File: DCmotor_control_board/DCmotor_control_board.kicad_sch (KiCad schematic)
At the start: 22 parts, among them J1 Conn_01x02_Pin, J10 Conn_01x04_Pin, J2 Conn_01x02_Pin, J7 Conn_01x02_Pin, U1 TB67H450FNG_EL, U3 L7805CV

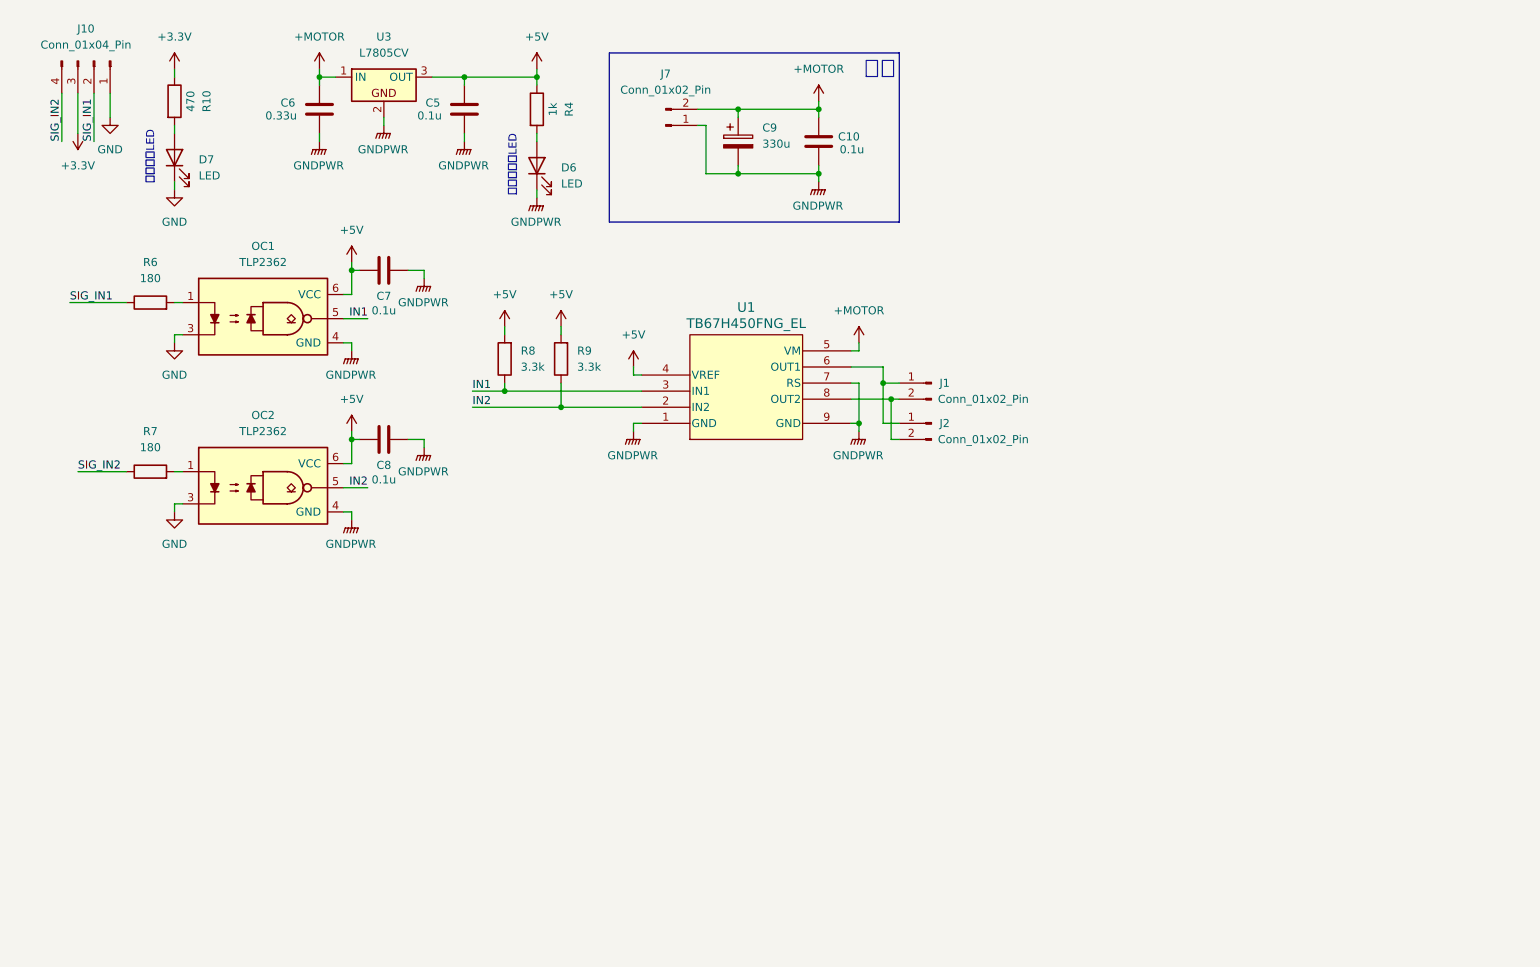
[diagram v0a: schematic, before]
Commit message: モータドライバ回路　回路図改良，フォトカプラの変更等
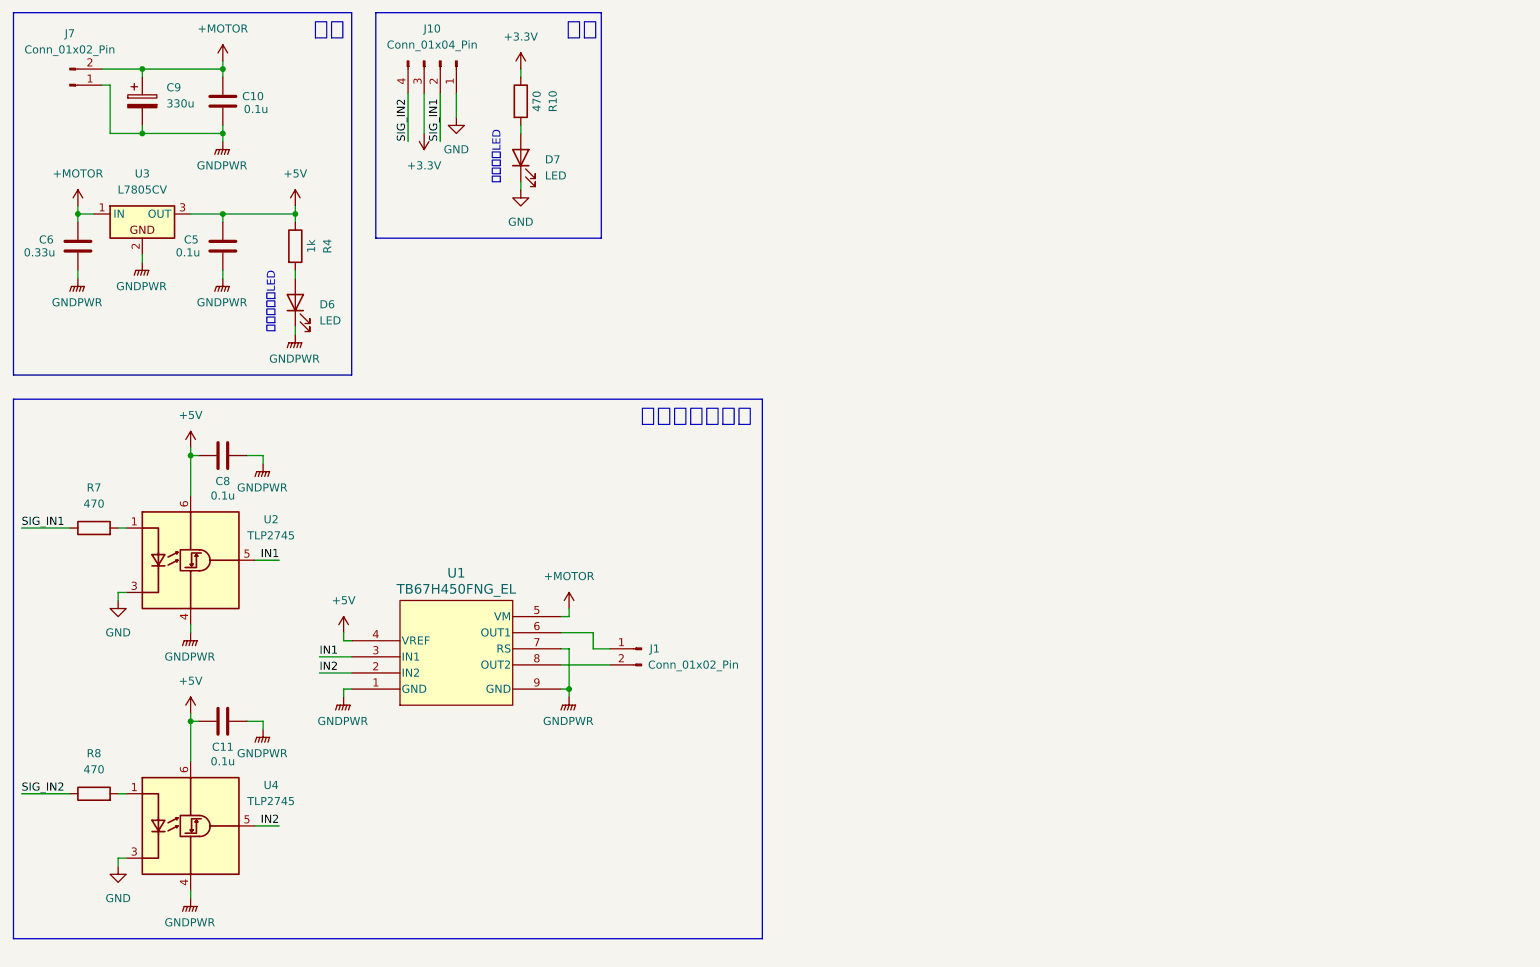
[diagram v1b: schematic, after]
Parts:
- removed C7: 0.1u, Capacitor_THT:C_Disc_D5.0mm_W2.5mm_P2.50mm, symbol Device:C
- removed J2: Conn_01x02_Pin, OU_connector:DF1E-2P-2.5DS, symbol Connector:Conn_01x02_Pin
- removed OC1, OC2: TLP2362, PCM_Package_SO_AKL:SO-5_4.4x3.6mm_P1.27mm, symbol PCM_Optocoupler_Logic_AKL:TLP2362
- removed R6: 180, Resistor_THT:R_Axial_DIN0207_L6.3mm_D2.5mm_P2.54mm_Vertical, symbol Device:R
- removed R9: 3.3k, Resistor_THT:R_Axial_DIN0207_L6.3mm_D2.5mm_P2.54mm_Vertical, symbol Device:R
- added C11: 0.1u, Capacitor_THT:C_Disc_D5.0mm_W2.5mm_P2.50mm, symbol Device:C
- added U2, U4: TLP2745, Package_SO:SO-6L_10x3.84mm_P1.27mm, symbol Isolator:TLP2745
- R7: value 180 -> 470; Buy_URL https://akizukidenshi.com/catalog/g/g125181/ -> https://akizukidenshi.com/catalog/g/g125471/
- R8: value 3.3k -> 470; Buy_URL https://akizukidenshi.com/catalog/g/g125332/ -> https://akizukidenshi.com/catalog/g/g125471/
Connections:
- net +5V: now also C11.2, U2.6 (VDD), U4.6 (VDD); no longer R8.2
- net GND: now also U2.3 (K), U4.3 (K)
- net GNDPWR: now also C11.1, U2.4 (GND), U4.4 (GND)
- net IN1: now also U2.5 (VO); no longer R8.1
- net IN2: now also U4.5 (VO)
- net SIG_IN1: now also R7.1
- net SIG_IN2: now also R8.1; no longer R7.1
- net at R7.2: now also U2.1 (A)
- new net: R8.2, U4.1 (A)
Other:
- note added: "モータドライバ"
- note added: "信号"
- moved on the sheet: C10, C5, C6, C8, C9, D6, D7, J1, J10, J7, R10, R4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

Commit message: モータドライバ基板　モータドライバを1系統から2系統に変更
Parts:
- removed D7: LED, LED_THT:LED_D5.0mm, symbol Device:LED
- removed R10: 470, Resistor_THT:R_Axial_DIN0207_L6.3mm_D2.5mm_P2.54mm_Vertical, symbol Device:R
- added C7, C8: 0.1u, Capacitor_THT:C_Disc_D5.0mm_W2.5mm_P2.50mm, symbol Device:C
- added J4: Conn_01x04_Pin, OU_connector:DF1E-4P-2.5DS, symbol Connector:Conn_01x04_Pin
- added J5: Conn_01x02_Pin, OU_connector:DF1E-2P-2.5DS, symbol Connector:Conn_01x02_Pin
- added R4, R5: 470, Resistor_THT:R_Axial_DIN0207_L6.3mm_D2.5mm_P2.54mm_Vertical, symbol Device:R
- added U5, U6: TLP2745, Package_SO:SO-6L_10x3.84mm_P1.27mm, symbol Isolator:TLP2745
- added U7: TB67H450FNG_EL, OU_Power:P-HSOP8-0405-1p27-002_TOS-L, symbol OU_Power:TB67H450FNG_EL
- renumbered C6 to C1, C9 to C2, C10 to C3, C5 to C4, C8 to C5, C11 to C6, D6 to D1, J7 to J1, J10 to J2, J1 to J3, R7 to R1, R8 to R2, R4 to R3, U3 to U1, U4 to U3, U1 to U4
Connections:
- net +5V: now also C7.2, C8.2, U5.6 (VDD), U6.6 (VDD), U7.4 (VREF)
- net +MOTOR: now also U7.5 (VM)
- net GNDPWR: now also C7.1, C8.1, U5.4 (GND), U6.4 (GND), U7.1 (GND), U7.7 (RS), U7.9 (GND)
- net +3.3V: no longer names the net of J2.3 (Pin_3)
- net GND renamed GND1
- net IN1 renamed IN1_1
- net IN2 renamed IN1_2
- new net: J5.1 (Pin_1), U7.6 (OUT1)
- new net: J5.2 (Pin_2), U7.8 (OUT2)
- new net: R5.2, U6.1 (A)
- new net: R4.2, U5.1 (A)
- new net GND2: J4.1 (Pin_1), U5.3 (K), U6.3 (K)
- new net IN2_1: U5.5 (VO), U7.3 (IN1)
- new net IN2_2: U6.5 (VO), U7.2 (IN2)
- new net SIG_IN3: J4.2 (Pin_2), R4.1
- new net SIG_IN4: J4.4 (Pin_4), R5.1
- no-connect marks 0 -> 2
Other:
- note added: "モータドライバ CH1"
- note added: "モータドライバ CH2"
- note removed: "モータドライバ"
- note removed: "制御電源LED"
- moved on the sheet: C5, C6, J3, R1, R2, U2, U3, U4

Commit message: モータドライバ基板　基板完成，ver 0.1
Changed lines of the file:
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@@
-		)
-	)
-	(label "IN1_2"
-		(at 64.77 73.66 0)
-		(effects
-			(font
-				(size 1.27 1.27)
-			)
-			(justify left bottom)
 		)
 	)

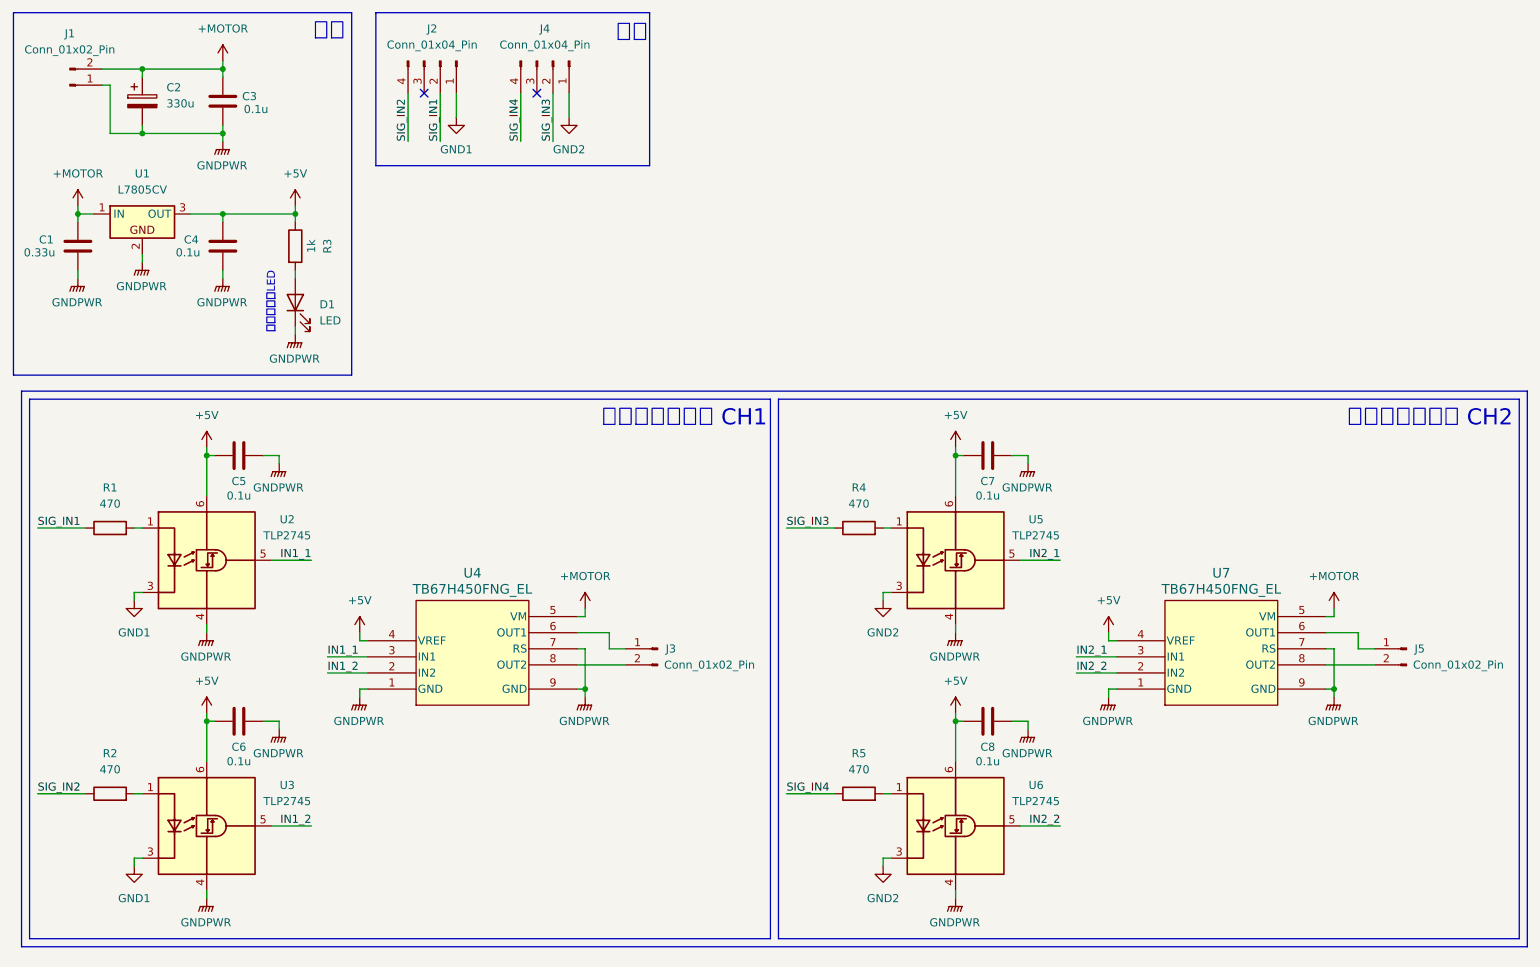
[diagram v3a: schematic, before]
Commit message: モータドライバ基板　TLP2745のURLを追加
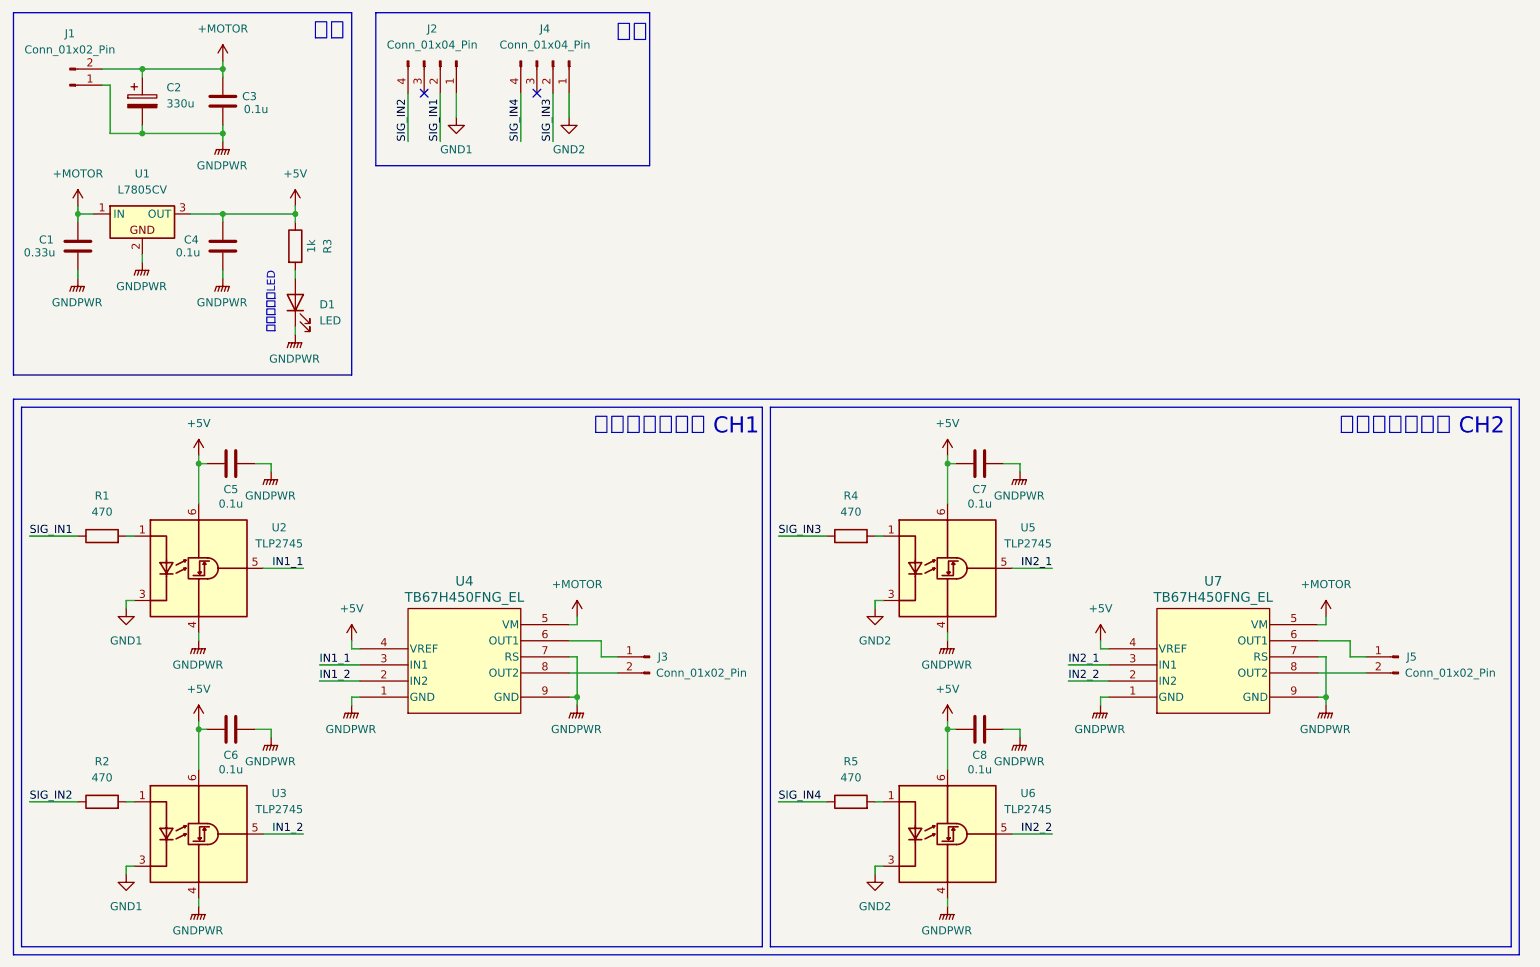
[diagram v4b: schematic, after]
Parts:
- U2, U3, U5, U6: Buy_URL (none) -> https://akizukidenshi.com/catalog/g/g118360/
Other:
- moved on the sheet: C5, C6, C7, C8, J3, J5, R1, R2, R4, R5, U2, U3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

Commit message: モータドライバ基板　シルクを一部修正，ver 1.0
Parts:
- renumbered J4 to J3, J3 to J4
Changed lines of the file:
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@@
 		(dnp no)
 		(fields_autoplaced yes)
-		(property "Reference" "#PWR022"
+		(property "Reference" "#PWR025"
 			(at 161.29 87.63 0)
 			(hide yes)
@@
 			(project "DCmotor_control_board"
 				(path "/99a91a5e-5cbb-4f6e-aa08-d3fc2ac4ed72"
-					(reference "#PWR022")
+					(reference "#PWR025")
 					(unit 1)
 				)
@@
 		(dnp no)
 		(fields_autoplaced yes)
-		(property "Reference" "#PWR020"
+		(property "Reference" "#PWR019"
 			(at 83.82 36.83 0)
 			(hide yes)
@@
 			(project "DCmotor_control_board"
 				(path "/99a91a5e-5cbb-4f6e-aa08-d3fc2ac4ed72"
-					(reference "#PWR020")
+					(reference "#PWR019")
 					(unit 1)
 				)
@@
 		(in_pos_files yes)
 		(dnp no)
-		(property "Reference" "J3"
+		(property "Reference" "J4"
 			(at 115.57 115.57 0)
 			(show_name no)
@@
 			(project "DCmotor_control_board"
 				(path "/99a91a5e-5cbb-4f6e-aa08-d3fc2ac4ed72"
-					(reference "J3")
+					(reference "J4")
 					(unit 1)
 				)
@@
 		(dnp no)
 		(fields_autoplaced yes)
-		(property "Reference" "#PWR023"
+		(property "Reference" "#PWR021"
 			(at 102.87 113.03 0)
 			(hide yes)
@@
 			(project "DCmotor_control_board"
 				(path "/99a91a5e-5cbb-4f6e-aa08-d3fc2ac4ed72"
-					(reference "#PWR023")
+					(reference "#PWR021")
 					(unit 1)
 				)
@@
 		(dnp no)
 		(fields_autoplaced yes)
-		(property "Reference" "#PWR021"
+		(property "Reference" "#PWR024"
 			(at 149.86 156.21 0)
 			(hide yes)
@@
 			(project "DCmotor_control_board"
 				(path "/99a91a5e-5cbb-4f6e-aa08-d3fc2ac4ed72"
-					(reference "#PWR021")
+					(reference "#PWR024")
 					(unit 1)
 				)
@@
 		(dnp no)
 		(fields_autoplaced yes)
-		(property "Reference" "#PWR025"
+		(property "Reference" "#PWR026"
 			(at 161.29 118.11 0)
 			(hide yes)
@@
 			(project "DCmotor_control_board"
 				(path "/99a91a5e-5cbb-4f6e-aa08-d3fc2ac4ed72"
-					(reference "#PWR025")
+					(reference "#PWR026")
 					(unit 1)
 				)
@@
 		(dnp no)
 		(fields_autoplaced yes)
-		(property "Reference" "#PWR019"
+		(property "Reference" "#PWR023"
 			(at 149.86 114.3 0)
 			(hide yes)
@@
 			(project "DCmotor_control_board"
 				(path "/99a91a5e-5cbb-4f6e-aa08-d3fc2ac4ed72"
-					(reference "#PWR019")
+					(reference "#PWR023")
 					(unit 1)
 				)
@@
 		(dnp no)
 		(fields_autoplaced yes)
-		(property "Reference" "J4"
+		(property "Reference" "J3"
 			(at 97.79 16.51 90)
 			(show_name no)
@@
 			(project "DCmotor_control_board"
 				(path "/99a91a5e-5cbb-4f6e-aa08-d3fc2ac4ed72"
-					(reference "J4")
+					(reference "J3")
 					(unit 1)
 				)
@@
 		(dnp no)
 		(fields_autoplaced yes)
-		(property "Reference" "#PWR024"
+		(property "Reference" "#PWR022"
 			(at 102.87 128.27 0)
 			(hide yes)
@@
 			(project "DCmotor_control_board"
 				(path "/99a91a5e-5cbb-4f6e-aa08-d3fc2ac4ed72"
-					(reference "#PWR024")
+					(reference "#PWR022")
 					(unit 1)
 				)
@@
 		(dnp no)
 		(fields_autoplaced yes)
-		(property "Reference" "#PWR026"
+		(property "Reference" "#PWR020"
 			(at 101.6 36.83 0)
 			(hide yes)
@@
 			(project "DCmotor_control_board"
 				(path "/99a91a5e-5cbb-4f6e-aa08-d3fc2ac4ed72"
-					(reference "#PWR026")
+					(reference "#PWR020")
 					(unit 1)
 				)
